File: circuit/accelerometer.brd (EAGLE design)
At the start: 100 x 80 mm, 10 parts, among them IC1 MIC5219BM5, U1 MMA8452Q

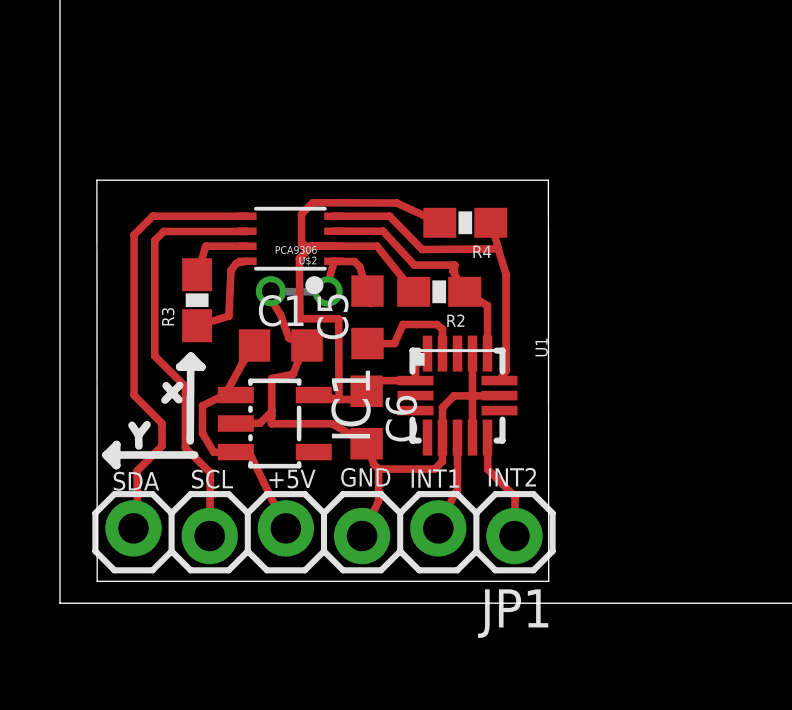
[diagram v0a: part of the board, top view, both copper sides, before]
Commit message: changing accelerometer, adding hooked up address pins
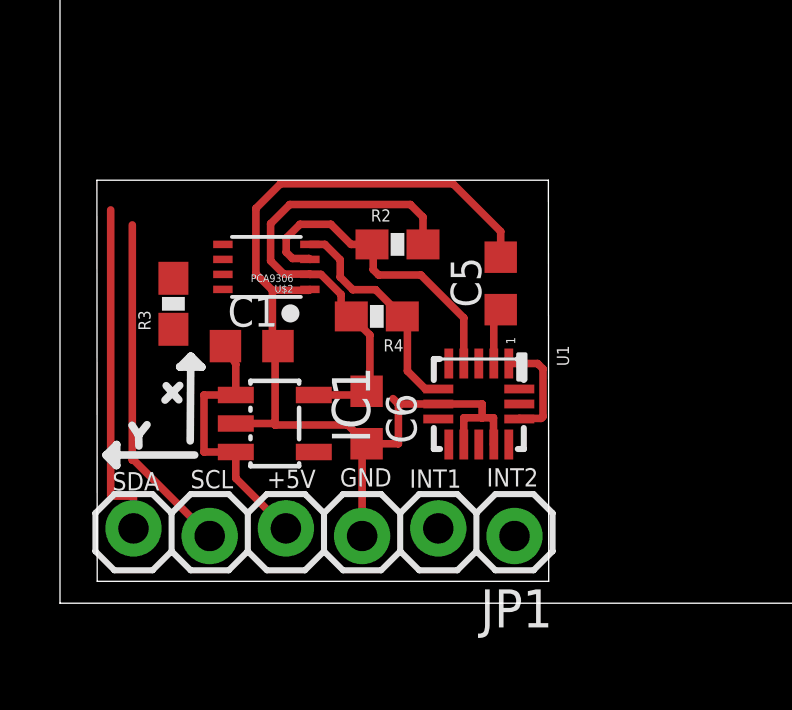
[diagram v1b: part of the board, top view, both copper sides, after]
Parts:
- moved C5 4.58 mm to (14.7, 10.7)
- moved R4 4.29 mm to (10.6, 9.56)
- moved R2 2.10 mm to (11.2, 12.0), turned to 0 degrees
- moved U$2 1.23 mm to (6.88, 11.2)
- moved C1 0.97 mm to (6.39, 8.57)
- moved R3 0.80 mm to (3.78, 9.98)
- moved U1 0.76 mm to (14.0, 6.64)
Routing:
- net GND: track 28.1 -> 35.4 mm, vias 2 -> 0
- net SDA_3: track 11.4 -> 7.58 mm
- net INT2: track 3.66 -> 0.00 mm
- net N$4: track 3.29 -> 0.00 mm
- net INT1: track 3.18 -> 0.00 mm
- net SDA_5: track 14.5 -> 11.4 mm
- net 3.3V: track 22.7 -> 19.7 mm
- net SCL_3: track 8.08 -> 10.8 mm
- net 5V: track 2.36 -> 0.00 mm
- net SCL_5: track 13.8 -> 11.5 mm
- net N$1: track 4.14 -> 1.89 mm
